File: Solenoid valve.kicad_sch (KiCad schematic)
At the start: 23 parts, among them J1 Conn_01x02, J2 Conn_01x02, J3 Conn_01x02, Q1 8050, Q2 CSD18540Q5B, U1 EL357N, U2 LM5060

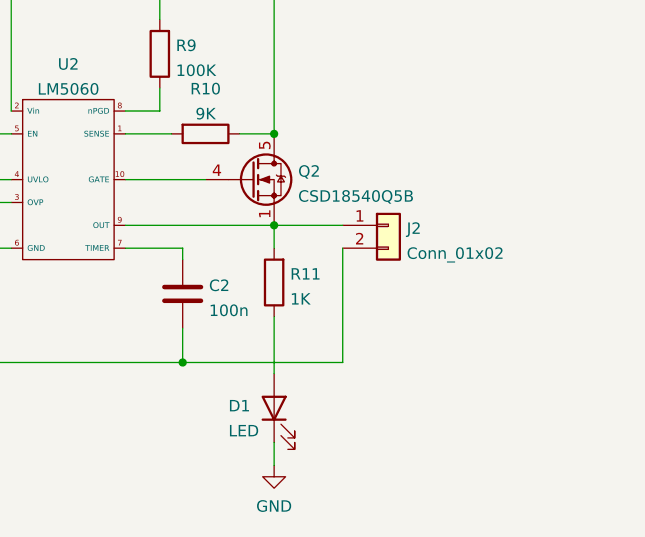
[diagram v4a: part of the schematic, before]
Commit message: Add protection for OUT
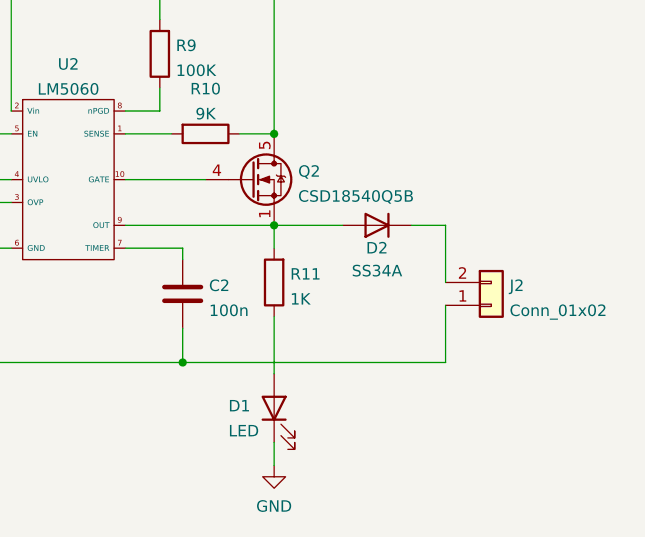
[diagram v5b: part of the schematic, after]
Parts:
- added D2: SS34A, Diode_SMD:D_SMA, symbol Device:D
- D1: footprint Diode_SMD:D_0603_1608Metric -> LED_SMD:LED_0603_1608Metric
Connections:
- net GND: now also J2.1 (Pin_2); no longer J2.2 (Pin_2)
- net at Q2.1 (S), Q2.2 (S), Q2.3 (S)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: now also D2.2 (A); no longer J2.1 (Pin_1)
- new net: D2.1 (K), J2.2 (Pin_1)
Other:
- moved on the sheet: J2
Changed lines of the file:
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@@
+    (stroke (width 0) (type default) (color 0 0 0 0))
+  )
+  (wire (pts (xy 186.69 144.78) (xy 190.5 144.78))
     (stroke (width 0) (type default) (color 0 0 0 0))
   )
@@
     (stroke (width 0) (type default) (color 0 0 0 0))
   )
-  (wire (pts (xy 179.07 147.32) (xy 179.07 160.02))
-    (stroke (width 0) (type default) (color 0 0 0 0))
-  )
   (wire (pts (xy 171.45 105.41) (xy 171.45 101.6))
     (stroke (width 0) (type default) (color 0 0 0 0))
@@
     (stroke (width 0) (type default) (color 0 0 0 0))
   )
+  (wire (pts (xy 190.5 144.78) (xy 190.5 151.13))
+    (stroke (width 0) (type default) (color 0 0 0 0))
+  )
   (wire (pts (xy 133.35 139.7) (xy 142.24 139.7))
     (stroke (width 0) (type default) (color 0 0 0 0))
   )
+  (wire (pts (xy 171.45 144.78) (xy 179.07 144.78))
+    (stroke (width 0) (type default) (color 0 0 0 0))
+  )
   (wire (pts (xy 72.39 152.4) (xy 72.39 144.78))
     (stroke (width 0) (type default) (color 0 0 0 0))
@@
     (stroke (width 0) (type default) (color 0 0 0 0))
   )
+  (wire (pts (xy 190.5 153.67) (xy 190.5 160.02))
+    (stroke (width 0) (type default) (color 0 0 0 0))
+  )
   (wire (pts (xy 158.75 115.57) (xy 171.45 115.57))
     (stroke (width 0) (type default) (color 0 0 0 0))
   )
-  (wire (pts (xy 161.29 160.02) (xy 179.07 160.02))
+  (wire (pts (xy 161.29 160.02) (xy 190.5 160.02))
     (stroke (width 0) (type default) (color 0 0 0 0))
   )
   (wire (pts (xy 104.14 160.02) (xy 104.14 163.83))
-    (stroke (width 0) (type default) (color 0 0 0 0))
-  )
-  (wire (pts (xy 171.45 144.78) (xy 179.07 144.78))
     (stroke (width 0) (type default) (color 0 0 0 0))
   )
@@
     (pin "2")
   )
+  (symbol (lib_id "Device:D") (at 182.88 144.78 180) (unit 1)
+    (in_bom yes) (on_board yes)
+    (property "Reference" "D2" (id 0) (at 182.88 147.32 0))
+    (property "Value" "SS34A" (id 1) (at 182.88 149.86 0))
+    (property "Footprint" "Diode_SMD:D_SMA" (id 2) (at 182.88 144.78 0)
+      (effects (font (size 1.27 1.27)) hide)
+    )
+    (property "Datasheet" "~" (id 3) (at 182.88 144.78 0)
+      (effects (font (size 1.27 1.27)) hide)
+    )
+    (pin "1")
+    (pin "2")
+  )
   (symbol (lib_id "power:GND") (at 171.45 171.45 0) (unit 1)
     (in_bom yes) (on_board yes) (fields_autoplaced)
@@
       (effects (font (size 1.27 1.27)) (justify right))
     )
-    (property "Footprint" "Diode_SMD:D_0603_1608Metric" (id 2) (at 171.45 165.1 0)
+    (property "Footprint" "LED_SMD:LED_0603_1608Metric" (id 2) (at 171.45 165.1 0)
       (effects (font (size 1.27 1.27)) hide)
     )
@@
     (pin "2")
   )
-  (symbol (lib_id "Connector_Generic:Conn_01x02") (at 184.15 144.78 0) (unit 1)
-    (in_bom yes) (on_board yes) (fields_autoplaced)
-    (property "Reference" "J2" (id 0) (at 186.182 145.1415 0)
-      (effects (font (size 1.27 1.27)) (justify left))
-    )
-    (property "Value" "Conn_01x02" (id 1) (at 186.182 147.9166 0)
-      (effects (font (size 1.27 1.27)) (justify left))
-    )
-    (property "Footprint" "Connector_AMASS:AMASS_XT30UPB-F_1x02_P5.0mm_Vertical" (id 2) (at 184.15 144.78 0)
-      (effects (font (size 1.27 1.27)) hide)
-    )
-    (property "Datasheet" "~" (id 3) (at 184.15 144.78 0)
+  (symbol (lib_name "Conn_01x02_1") (lib_id "Connector_Generic:Conn_01x02") (at 195.58 151.13 0) (unit 1)
+    (in_bom yes) (on_board yes) (fields_autoplaced)
+    (property "Reference" "J2" (id 0) (at 197.612 151.4915 0)
+      (effects (font (size 1.27 1.27)) (justify left))
+    )
+    (property "Value" "Conn_01x02" (id 1) (at 197.612 154.2666 0)
+      (effects (font (size 1.27 1.27)) (justify left))
+    )
+    (property "Footprint" "Connector_AMASS:AMASS_XT30UPB-F_1x02_P5.0mm_Vertical" (id 2) (at 195.58 148.59 0)
+      (effects (font (size 1.27 1.27)) hide)
+    )
+    (property "Datasheet" "~" (id 3) (at 195.58 151.13 0)
       (effects (font (size 1.27 1.27)) hide)
     )
@@
     )
     (path "/cc716bd0-4abf-43b4-b162-4586fc1a08aa"
-      (reference "D1") (unit 1) (value "LED") (footprint "Diode_SMD:D_0603_1608Metric")
+      (reference "D1") (unit 1) (value "LED") (footprint "LED_SMD:LED_0603_1608Metric")
+    )
+    (path "/5a2e5954-8ae3-4771-b360-5c413b28053d"
+      (reference "D2") (unit 1) (value "SS34A") (footprint "Diode_SMD:D_SMA")
     )
     (path "/dc84a8e7-f98b-48ce-82ce-407eb30f63c7"

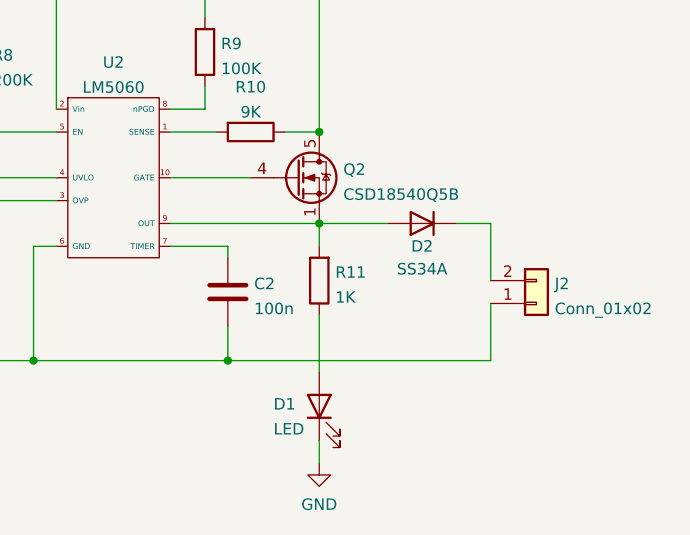
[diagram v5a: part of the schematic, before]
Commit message: Add a mimic ss34a on the top
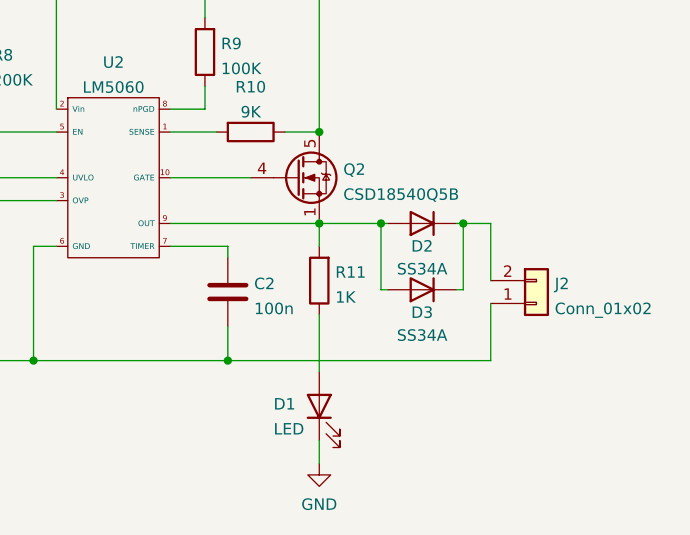
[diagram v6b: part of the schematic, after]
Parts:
- added D3: SS34A, Diode_SMD:D_SMA, symbol Device:D
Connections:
- net at D2.2 (A), Q2.1 (S), Q2.2 (S)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: now also D3.2 (A)
- net at D2.1 (K), J2.2 (Pin_1): now also D3.1 (K)

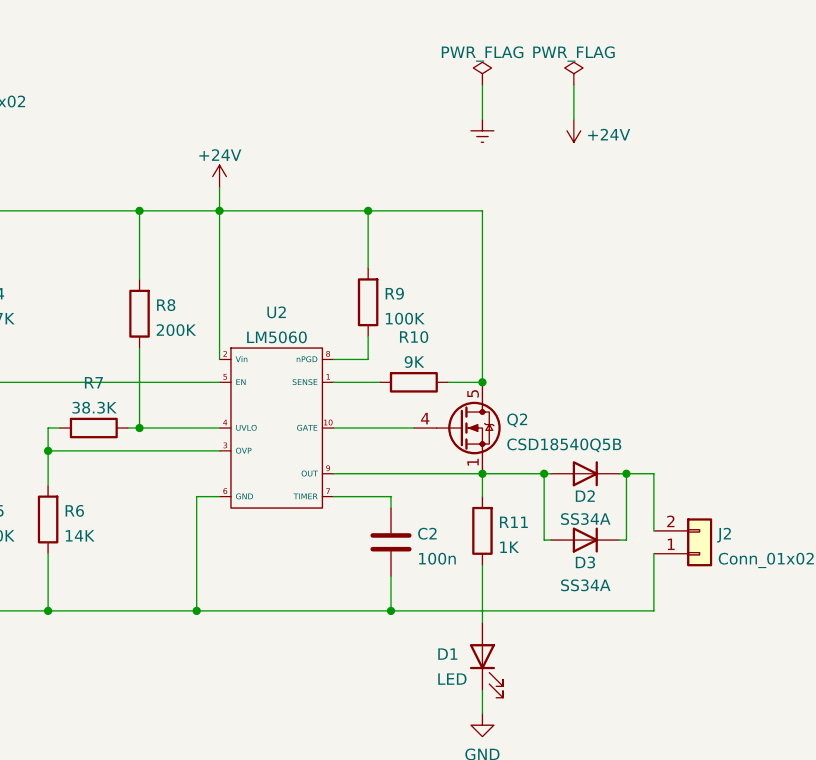
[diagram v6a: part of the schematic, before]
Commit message: Add a 24V voltage regulator diode
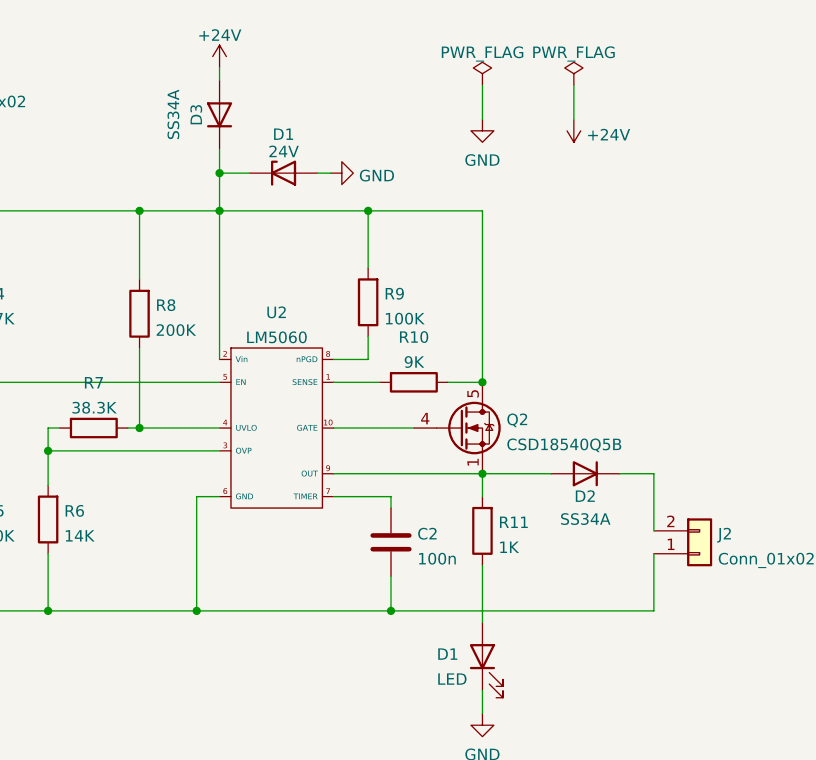
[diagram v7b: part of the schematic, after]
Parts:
- added D1: 24V, Diode_SMD:D_SOD-123, symbol Diode:BZT52Bxx
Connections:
- net +24V: now also D3.2 (A); no longer Q2.5 (D), R1.2, R10.1, R4.2, R8.2, R9.2, U2.2 (Vin)
- net GND: now also D1.2 (A)
- net at D2.2 (A), Q2.1 (S), Q2.2 (S)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: no longer D3.2 (A)
- net at D2.1 (K), J2.2 (Pin_1): no longer D3.1 (K)
- new net: D1.1 (K), D3.1 (K), Q2.5 (D), R1.2, R10.1, R4.2, R8.2, R9.2, U2.2 (Vin)
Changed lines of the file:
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@@
   (junction (at 171.45 144.78) (diameter 0) (color 0 0 0 0)
   )
-  (junction (at 178.308 144.78) (diameter 0) (color 0 0 0 0)
-  )
-  (junction (at 187.452 144.78) (diameter 0) (color 0 0 0 0)
-  )
   (junction (at 87.63 160.02) (diameter 0) (color 0 0 0 0)
   )
@@
   (junction (at 123.19 160.02) (diameter 0) (color 0 0 0 0)
   )
+  (junction (at 142.24 111.379) (diameter 0) (color 0 0 0 0)
+  )
   (wire (pts (xy 133.35 115.57) (xy 142.24 115.57))
     (stroke (width 0) (type default))
@@
     (stroke (width 0) (type default))
   )
-  (wire (pts (xy 142.24 113.03) (xy 142.24 115.57))
+  (wire (pts (xy 145.542 111.379) (xy 142.24 111.379))
     (stroke (width 0) (type default))
   )
@@
     (stroke (width 0) (type default))
   )
+  (wire (pts (xy 142.24 99.695) (xy 142.24 101.092))
+    (stroke (width 0) (type default))
+  )
   (wire (pts (xy 181.61 105.41) (xy 181.61 101.6))
     (stroke (width 0) (type default))
@@
     (stroke (width 0) (type default))
   )
-  (wire (pts (xy 178.308 144.78) (xy 179.07 144.78))
-    (stroke (width 0) (type default))
-  )
   (wire (pts (xy 57.15 157.48) (xy 40.64 157.48))
     (stroke (width 0) (type default))
@@
     (stroke (width 0) (type default))
   )
-  (wire (pts (xy 186.69 144.78) (xy 187.452 144.78))
+  (wire (pts (xy 186.69 144.78) (xy 190.5 144.78))
     (stroke (width 0) (type default))
   )
@@
     (stroke (width 0) (type default))
   )
+  (wire (pts (xy 154.559 111.379) (xy 153.162 111.379))
+    (stroke (width 0) (type default))
+  )
   (wire (pts (xy 161.29 156.21) (xy 161.29 160.02))
     (stroke (width 0) (type default))
@@
     (stroke (width 0) (type default))
   )
-  (wire (pts (xy 179.07 152.146) (xy 178.308 152.146))
-    (stroke (width 0) (type default))
-  )
   (wire (pts (xy 139.7 160.02) (xy 123.19 160.02))
     (stroke (width 0) (type default))
@@
     (stroke (width 0) (type default))
   )
-  (wire (pts (xy 178.308 144.78) (xy 178.308 152.146))
-    (stroke (width 0) (type default))
-  )
   (wire (pts (xy 114.3 134.62) (xy 104.14 134.62))
     (stroke (width 0) (type default))
@@
     (stroke (width 0) (type default))
   )
-  (wire (pts (xy 187.452 152.146) (xy 187.452 144.78))
-    (stroke (width 0) (type default))
-  )
   (wire (pts (xy 114.3 153.67) (xy 114.3 160.02))
     (stroke (width 0) (type default))
@@
     (stroke (width 0) (type default))
   )
+  (wire (pts (xy 142.24 108.712) (xy 142.24 111.379))
+    (stroke (width 0) (type default))
+  )
   (wire (pts (xy 102.87 105.41) (xy 102.87 102.87))
     (stroke (width 0) (type default))
@@
     (stroke (width 0) (type default))
   )
-  (wire (pts (xy 186.69 152.146) (xy 187.452 152.146))
-    (stroke (width 0) (type default))
-  )
   (wire (pts (xy 133.35 115.57) (xy 133.35 123.19))
     (stroke (width 0) (type default))
@@
     (stroke (width 0) (type default))
   )
-  (wire (pts (xy 187.452 144.78) (xy 190.5 144.78))
-    (stroke (width 0) (type default))
-  )
-  (wire (pts (xy 171.45 144.78) (xy 178.308 144.78))
+  (wire (pts (xy 171.45 144.78) (xy 179.07 144.78))
     (stroke (width 0) (type default))
   )
@@
     (stroke (width 0) (type default))
   )
+  (wire (pts (xy 142.24 111.379) (xy 142.24 115.57))
+    (stroke (width 0) (type default))
+  )
   (wire (pts (xy 40.64 157.48) (xy 40.64 156.21))
     (stroke (width 0) (type default))
@@
     )
   )
+  (symbol (lib_id "Diode:BZT52Bxx") (at 149.352 111.379 0) (unit 1)
+    (in_bom yes) (on_board yes) (dnp no) (fields_autoplaced)
+    (property "Reference" "D1" (at 149.352 107.0991 0)
+      (effects (font (size 1.27 1.27)))
+    )
+    (property "Value" "24V" (at 149.352 109.0201 0)
+      (effects (font (size 1.27 1.27)))
+    )
+    (property "Footprint" "Diode_SMD:D_SOD-123" (at 149.352 115.824 0)
+      (effects (font (size 1.27 1.27)) hide)
+    )
+    (property "Datasheet" "https://diotec.com/tl_files/diotec/files/pdf/datasheets/bzt52b2v4.pdf" (at 149.352 111.379 0)
+      (effects (font (size 1.27 1.27)) hide)
+    )
+    (pin "1")
+    (pin "2")
+    (instances
+      (project "NMOS_SWITCH"
+        (path "/4ad7c0a0-4add-45a6-8449-3f0564e8213d"
+          (reference "D1") (unit 1)
+        )
+      )
+      (project "Solenoid valve"
+        (path "/e63e39d7-6ac0-4ffd-8aa3-1841a4541b55"
+          (reference "D4") (unit 1)
+        )
+      )
+    )
+  )
   (symbol (lib_id "power:PWR_FLAG") (at 181.61 101.6 0) (unit 1)
     (in_bom yes) (on_board yes) (dnp no) (fields_autoplaced)
@@
     )
   )
-  (symbol (lib_id "power:Earth") (at 171.45 105.41 0) (unit 1)
-    (in_bom yes) (on_board yes) (dnp no) (fields_autoplaced)
-    (property "Reference" "#PWR05" (at 171.45 111.76 0)
-      (effects (font (size 1.27 1.27)) hide)
-    )
-    (property "Value" "Earth" (at 171.45 109.22 0)
-      (effects (font (size 1.27 1.27)) hide)
-    )
-    (property "Footprint" "" (at 171.45 105.41 0)
-      (effects (font (size 1.27 1.27)) hide)
-    )
-    (property "Datasheet" "~" (at 171.45 105.41 0)
-      (effects (font (size 1.27 1.27)) hide)
-    )
-    (pin "1")
-    (instances
-      (project "Solenoid valve"
-        (path "/e63e39d7-6ac0-4ffd-8aa3-1841a4541b55"
-          (reference "#PWR05") (unit 1)
+  (symbol (lib_id "power:GND") (at 154.559 111.379 90) (unit 1)
+    (in_bom yes) (on_board yes) (dnp no) (fields_autoplaced)
+    (property "Reference" "#PWR03" (at 160.909 111.379 0)
+      (effects (font (size 1.27 1.27)) hide)
+    )
+    (property "Value" "GND" (at 157.734 111.6958 90)
+      (effects (font (size 1.27 1.27)) (justify right))
+    )
+    (property "Footprint" "" (at 154.559 111.379 0)
+      (effects (font (size 1.27 1.27)) hide)
+    )
+    (property "Datasheet" "" (at 154.559 111.379 0)
+      (effects (font (size 1.27 1.27)) hide)
+    )
+    (pin "1")
+    (instances
+      (project "Solenoid valve"
+        (path "/e63e39d7-6ac0-4ffd-8aa3-1841a4541b55"
+          (reference "#PWR03") (unit 1)
         )
       )
@@
     )
   )
-  (symbol (lib_id "power:+24V") (at 142.24 113.03 0) (unit 1)
-    (in_bom yes) (on_board yes) (dnp no) (fields_autoplaced)
-    (property "Reference" "#PWR0101" (at 142.24 116.84 0)
-      (effects (font (size 1.27 1.27)) hide)
-    )
-    (property "Value" "+24V" (at 142.24 109.4255 0)
-      (effects (font (size 1.27 1.27)))
-    )
-    (property "Footprint" "" (at 142.24 113.03 0)
-      (effects (font (size 1.27 1.27)) hide)
-    )
-    (property "Datasheet" "" (at 142.24 113.03 0)
+  (symbol (lib_id "power:+24V") (at 142.24 99.695 0) (unit 1)
+    (in_bom yes) (on_board yes) (dnp no) (fields_autoplaced)
+    (property "Reference" "#PWR0101" (at 142.24 103.505 0)
+      (effects (font (size 1.27 1.27)) hide)
+    )
+    (property "Value" "+24V" (at 142.24 96.0905 0)
+      (effects (font (size 1.27 1.27)))
+    )
+    (property "Footprint" "" (at 142.24 99.695 0)
+      (effects (font (size 1.27 1.27)) hide)
+    )
+    (property "Datasheet" "" (at 142.24 99.695 0)
       (effects (font (size 1.27 1.27)) hide)
     )
@@
         (path "/e63e39d7-6ac0-4ffd-8aa3-1841a4541b55"
           (reference "#PWR0101") (unit 1)
+        )
+      )
+    )
+  )
+  (symbol (lib_id "power:GND") (at 171.45 105.41 0) (unit 1)
+    (in_bom yes) (on_board yes) (dnp no) (fields_autoplaced)
+    (property "Reference" "#PWR01" (at 171.45 111.76 0)
+      (effects (font (size 1.27 1.27)) hide)
+    )
+    (property "Value" "GND" (at 171.45 109.9725 0)
+      (effects (font (size 1.27 1.27)))
+    )
+    (property "Footprint" "" (at 171.45 105.41 0)
+      (effects (font (size 1.27 1.27)) hide)
+    )
+    (property "Datasheet" "" (at 171.45 105.41 0)
+      (effects (font (size 1.27 1.27)) hide)
+    )
+    (pin "1")
+    (instances
+      (project "Solenoid valve"
+        (path "/e63e39d7-6ac0-4ffd-8aa3-1841a4541b55"
+          (reference "#PWR01") (unit 1)
         )
       )
@@
     )
   )
-  (symbol (lib_id "Device:D") (at 182.88 152.146 180) (unit 1)
-    (in_bom yes) (on_board yes) (dnp no)
-    (property "Reference" "D3" (at 182.88 154.686 0)
-      (effects (font (size 1.27 1.27)))
-    )
-    (property "Value" "SS34A" (at 182.88 157.226 0)
-      (effects (font (size 1.27 1.27)))
-    )
-    (property "Footprint" "Diode_SMD:D_SMA" (at 182.88 152.146 0)
-      (effects (font (size 1.27 1.27)) hide)
-    )
-    (property "Datasheet" "~" (at 182.88 152.146 0)
-      (effects (font (size 1.27 1.27)) hide)
-    )
-    (pin "1")
-    (pin "2")
-    (instances
-      (project "Solenoid valve"
-        (path "/e63e39d7-6ac0-4ffd-8aa3-1841a4541b55"
-          (reference "D3") (unit 1)
-        )
-      )
-    )
-  )
   (symbol (lib_id "power:+24V") (at 102.87 99.06 0) (unit 1)
     (in_bom yes) (on_board yes) (dnp no) (fields_autoplaced)
@@
         )
       )
+    )
+  )
+  (symbol (lib_id "Device:D") (at 142.24 104.902 90) (unit 1)
+    (in_bom yes) (on_board yes) (dnp no)
+    (property "Reference" "D3" (at 139.7 104.902 0)
+      (effects (font (size 1.27 1.27)))
+    )
+    (property "Value" "SS34A" (at 137.16 104.902 0)
+      (effects (font (size 1.27 1.27)))
+    )
+    (property "Footprint" "Diode_SMD:D_SMA" (at 142.24 104.902 0)
+      (effects (font (size 1.27 1.27)) hide)
+    )
+    (property "Datasheet" "~" (at 142.24 104.902 0)
+      (effects (font (size 1.27 1.27)) hide)
+    )
+    (pin "1")
+    (pin "2")
+    (instances
+      (project "Solenoid valve"
+        (path "/e63e39d7-6ac0-4ffd-8aa3-1841a4541b55"
+          (reference "D3") (unit 1)
+        )
+      )
